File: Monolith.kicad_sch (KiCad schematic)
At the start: 22 parts, among them J2 Conn_01x11, J3 Conn_01x11, J4 Conn_01x02, J5 Conn_01x02, J7 Conn_01x08, U1 ADS1299IPAGR, U12 ESP32-S3-MINI-1

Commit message: Replace volt reg
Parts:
- C3: footprint (none) -> Capacitor_SMD:C_0603_1608Metric
- R6: footprint (none) -> Resistor_SMD:R_0603_1608Metric
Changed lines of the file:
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@@
       (effects (font (size 1.27 1.27)) (justify left))
     )
-    (property "Footprint" "" (at 166.5224 43.0276 0)
+    (property "Footprint" "Capacitor_SMD:C_0603_1608Metric" (at 166.5224 43.0276 0)
       (effects (font (size 1.27 1.27)) hide)
     )
@@
       (effects (font (size 1.27 1.27)) (justify left))
     )
-    (property "Footprint" "" (at 163.5252 25.5524 90)
-      (effects (font (size 1.27 1.27)) hide)
-    )
+    (property "Footprint" "Resistor_SMD:R_0603_1608Metric" (at 163.5252 25.5524 90)
+      (effects (font (size 1.27 1.27)) hide)
+    )

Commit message: fixes
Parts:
- C20: value 1uF -> 0.1uF; LCSC C15849 -> C3011705
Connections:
- net AVSS: now also C32.1, C33.1, U1.25 (VREFN)
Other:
- moved on the sheet: C32, C33

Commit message: new fixes
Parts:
- added C4: 0.1uF, Capacitor_SMD:C_0603_1608Metric, symbol Device:C
- added C5: 1uF, Capacitor_SMD:C_0603_1608Metric, symbol Device:C
- added S1, S2: TS-1187A-B-A-B, TS-1187A-B-A-B:SW_TS-1187A-B-A-B, symbol TS-1187A-B-A-B:TS-1187A-B-A-B
- C1, C33: LCSC C1691 -> C96446
- C19: footprint Capacitor_SMD:C_0805_2012Metric -> Capacitor_SMD:C_1206_3216Metric; LCSC C141660 -> C15008
- C2, C20, C32, C34: LCSC C3011705 -> C14663
- C56: LCSC C106205 -> C1523
- R6: LCSC C98220 -> C25804
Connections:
- net GND: now also C4.1, C5.2, S2.C, S2.D
- net DN: now reaches U12.23 (GPIO19/U1RTS/ADC2_CH8/CLK_OUT2/USB_D-)
- net DP: now reaches U12.24 (GPIO20/U1CTS/ADC2_CH9/CLK_OUT1/USB_D+)
- net EN: no longer names the net of C3.1, R6.2, U12.45 (EN)
- net EN: now also S1.C, S1.D
- net GPIO0: no longer names the net of U12.4 (GPIO0/BOOT)
- net GPIO0: now also C4.2, S2.A, S2.B
- new net: C5.1, S1.A, S1.B
- no-connect marks 38 -> 36
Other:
- sheet USB Port ports: added DN, DP; removed CHIP_PU, IO0, RX, TX

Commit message: fix pin headers
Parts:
- J2, J3: footprint Connector_PinSocket_2.54mm:PinSocket_1x11_P2.54mm_Vertical -> Connector_PinHeader_2.54mm:PinHeader_1x11_P2.54mm_Vertical
- J4, J5: footprint Connector_PinSocket_2.54mm:PinSocket_1x02_P2.54mm_Vertical -> Connector_PinHeader_2.54mm:PinHeader_1x02_P2.54mm_Vertical
- J7: footprint Connector_PinHeader_2.54mm:PinHeader_1x08_P2.54mm_Vertical -> Connector_PinSocket_2.54mm:PinSocket_1x08_P2.54mm_Vertical
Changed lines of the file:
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@@
       (effects (font (size 1.27 1.27)) (justify left))
     )
-    (property "Footprint" "Connector_PinHeader_2.54mm:PinHeader_1x08_P2.54mm_Vertical" (at 264.795 152.4 0)
+    (property "Footprint" "Connector_PinSocket_2.54mm:PinSocket_1x08_P2.54mm_Vertical" (at 264.795 152.4 0)
       (effects (font (size 1.27 1.27)) hide)
     )
@@
       (effects (font (size 1.27 1.27)) (justify left))
     )
-    (property "Footprint" "Connector_PinSocket_2.54mm:PinSocket_1x02_P2.54mm_Vertical" (at 28.575 55.245 0)
+    (property "Footprint" "Connector_PinHeader_2.54mm:PinHeader_1x02_P2.54mm_Vertical" (at 28.575 55.245 0)
       (effects (font (size 1.27 1.27)) hide)
     )
@@
       (effects (font (size 1.27 1.27)))
     )
-    (property "Footprint" "Connector_PinSocket_2.54mm:PinSocket_1x11_P2.54mm_Vertical" (at 41.275 36.83 0)
+    (property "Footprint" "Connector_PinHeader_2.54mm:PinHeader_1x11_P2.54mm_Vertical" (at 41.275 36.83 0)
       (effects (font (size 1.27 1.27)) hide)
     )
@@
       (effects (font (size 1.27 1.27)))
     )
-    (property "Footprint" "Connector_PinSocket_2.54mm:PinSocket_1x11_P2.54mm_Vertical" (at 29.21 36.83 0)
+    (property "Footprint" "Connector_PinHeader_2.54mm:PinHeader_1x11_P2.54mm_Vertical" (at 29.21 36.83 0)
       (effects (font (size 1.27 1.27)) hide)
     )
@@
       (effects (font (size 1.27 1.27)) (justify left))
     )
-    (property "Footprint" "Connector_PinSocket_2.54mm:PinSocket_1x02_P2.54mm_Vertical" (at 28.575 62.23 0)
-      (effects (font (size 1.27 1.27)) hide)
-    )
+    (property "Footprint" "Connector_PinHeader_2.54mm:PinHeader_1x02_P2.54mm_Vertical" (at 28.575 62.23 0)
+      (effects (font (size 1.27 1.27)) hide)
+    )

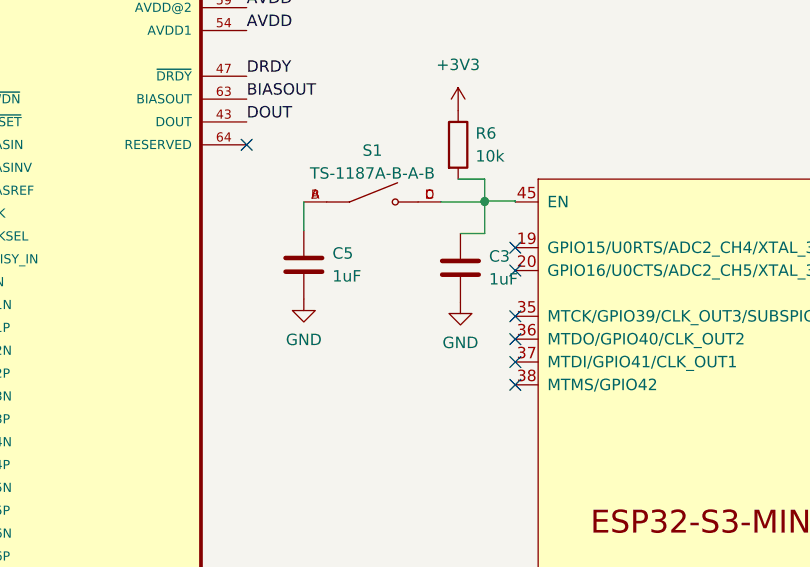
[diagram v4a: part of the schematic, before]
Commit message: fix reset button
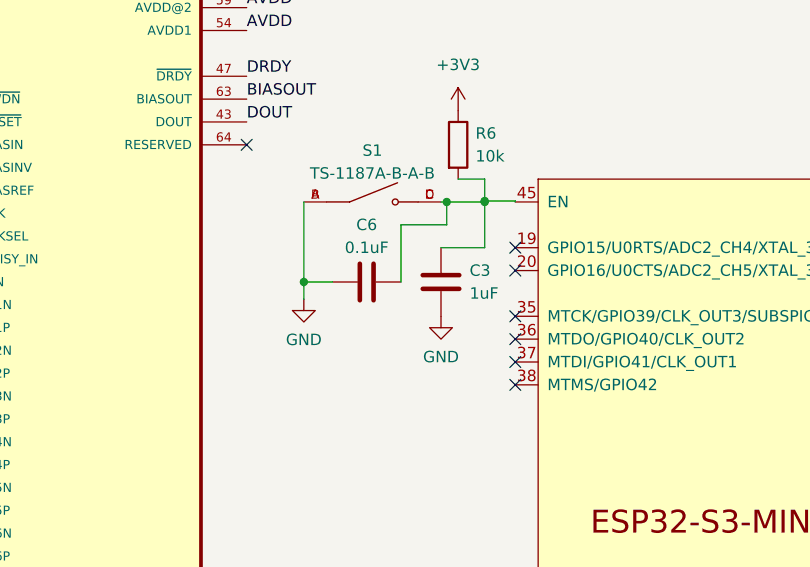
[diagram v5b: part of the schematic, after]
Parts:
- removed C5: 1uF, Capacitor_SMD:C_0603_1608Metric, symbol Device:C
- added C6: 0.1uF, Capacitor_SMD:C_0603_1608Metric, symbol Device:C
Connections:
- net GND: now also S1.A, S1.B, C6.2
- net at C3.1, R6.2, S1.C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: now also C6.1
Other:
- moved on the sheet: C3
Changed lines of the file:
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@@
   (junction (at 164.8714 53.34) (diameter 0) (color 0 0 0 0)
   )
+  (junction (at 144.78 62.23) (diameter 0) (color 0 0 0 0)
+  )
   (junction (at 164.8714 53.229) (diameter 0) (color 0 0 0 0)
   )
@@
   )
   (junction (at 74.93 50.165) (diameter 0) (color 0 0 0 0)
+  )
+  (junction (at 160.655 53.34) (diameter 0) (color 0 0 0 0)
   )
   (junction (at 144.78 143.51) (diameter 0) (color 0 0 0 0)
@@
     (stroke (width 0) (type default))
   )
+  (wire (pts (xy 160.655 55.88) (xy 155.575 55.88))
+    (stroke (width 0) (type default))
+  )
   (wire (pts (xy 261.62 68.58) (xy 259.715 68.58))
     (stroke (width 0) (type default))
   )
+  (wire (pts (xy 144.78 62.23) (xy 144.78 64.135))
+    (stroke (width 0) (type default))
+  )
   (wire (pts (xy 91.44 118.11) (xy 102.87 118.11))
     (stroke (width 0) (type default))
@@
     (stroke (width 0) (type default))
   )
-  (wire (pts (xy 164.8714 53.34) (xy 164.8714 56.8452))
+  (wire (pts (xy 164.8714 53.34) (xy 164.8714 58.42))
+    (stroke (width 0) (type default))
+  )
+  (wire (pts (xy 160.655 53.34) (xy 164.8714 53.34))
     (stroke (width 0) (type default))
   )
@@
     (stroke (width 0) (type default))
   )
+  (wire (pts (xy 147.955 62.23) (xy 144.78 62.23))
+    (stroke (width 0) (type default))
+  )
   (wire (pts (xy 213.995 31.75) (xy 213.995 43.18))
     (stroke (width 0) (type default))
@@
     (stroke (width 0) (type default))
   )
-  (wire (pts (xy 144.78 53.34) (xy 144.78 56.515))
+  (wire (pts (xy 144.78 53.34) (xy 144.78 62.23))
     (stroke (width 0) (type default))
   )
@@
     (stroke (width 0) (type default))
   )
-  (wire (pts (xy 162.179 56.8452) (xy 164.8714 56.8452))
+  (wire (pts (xy 160.02 58.42) (xy 164.8714 58.42))
+    (stroke (width 0) (type default))
+  )
+  (wire (pts (xy 155.575 55.88) (xy 155.575 62.23))
     (stroke (width 0) (type default))
   )
@@
     (stroke (width 0) (type default))
   )
+  (wire (pts (xy 160.655 53.34) (xy 160.655 55.88))
+    (stroke (width 0) (type default))
+  )
   (wire (pts (xy 164.8714 50.8) (xy 164.8714 53.229))
     (stroke (width 0) (type default))
@@
     (stroke (width 0) (type default))
   )
-  (wire (pts (xy 160.02 53.34) (xy 164.8714 53.34))
+  (wire (pts (xy 160.02 53.34) (xy 160.655 53.34))
     (stroke (width 0) (type default))
   )
@@
     )
   )
-  (symbol (lib_id "Device:C") (at 162.179 60.6552 0) (unit 1)
-    (in_bom yes) (on_board yes) (dnp no) (fields_autoplaced)
-    (property "Reference" "C3" (at 165.354 59.3852 0)
-      (effects (font (size 1.27 1.27)) (justify left))
-    )
-    (property "Value" "1uF" (at 165.354 61.9252 0)
-      (effects (font (size 1.27 1.27)) (justify left))
-    )
-    (property "Footprint" "Capacitor_SMD:C_0603_1608Metric" (at 163.1442 64.4652 0)
-      (effects (font (size 1.27 1.27)) hide)
-    )
-    (property "Datasheet" "~" (at 162.179 60.6552 0)
-      (effects (font (size 1.27 1.27)) hide)
-    )
-    (property "LCSC" "C15849" (at 162.179 60.6552 0)
+  (symbol (lib_id "Device:C") (at 160.02 62.23 0) (unit 1)
+    (in_bom yes) (on_board yes) (dnp no) (fields_autoplaced)
+    (property "Reference" "C3" (at 163.195 60.96 0)
+      (effects (font (size 1.27 1.27)) (justify left))
+    )
+    (property "Value" "1uF" (at 163.195 63.5 0)
+      (effects (font (size 1.27 1.27)) (justify left))
+    )
+    (property "Footprint" "Capacitor_SMD:C_0603_1608Metric" (at 160.9852 66.04 0)
+      (effects (font (size 1.27 1.27)) hide)
+    )
+    (property "Datasheet" "~" (at 160.02 62.23 0)
+      (effects (font (size 1.27 1.27)) hide)
+    )
+    (property "LCSC" "C15849" (at 160.02 62.23 0)
       (effects (font (size 1.27 1.27)) hide)
     )
@@
         (path "/a4ecfbe3-0f16-403e-8cdc-2760bb3b2c3f"
           (reference "C3") (unit 1)
+        )
+      )
+    )
+  )
+  (symbol (lib_id "Device:C") (at 151.765 62.23 270) (unit 1)
+    (in_bom yes) (on_board yes) (dnp no) (fields_autoplaced)
+    (property "Reference" "C6" (at 151.765 55.88 90)
+      (effects (font (size 1.27 1.27)))
+    )
+    (property "Value" "0.1uF" (at 151.765 58.42 90)
+      (effects (font (size 1.27 1.27)))
+    )
+    (property "Footprint" "Capacitor_SMD:C_0603_1608Metric" (at 147.955 63.1952 0)
+      (effects (font (size 1.27 1.27)) hide)
+    )
+    (property "Datasheet" "~" (at 151.765 62.23 0)
+      (effects (font (size 1.27 1.27)) hide)
+    )
+    (property "LCSC" "C14663" (at 151.765 62.23 90)
+      (effects (font (size 1.27 1.27)) hide)
+    )
+    (pin "1")
+    (pin "2")
+    (instances
+      (project "Monolith"
+        (path "/a4ecfbe3-0f16-403e-8cdc-2760bb3b2c3f"
+          (reference "C6") (unit 1)
         )
       )
@@
     )
   )
-  (symbol (lib_id "Device:C") (at 144.78 60.325 0) (unit 1)
-    (in_bom yes) (on_board yes) (dnp no) (fields_autoplaced)
-    (property "Reference" "C5" (at 147.955 59.055 0)
-      (effects (font (size 1.27 1.27)) (justify left))
-    )
-    (property "Value" "1uF" (at 147.955 61.595 0)
-      (effects (font (size 1.27 1.27)) (justify left))
-    )
-    (property "Footprint" "Capacitor_SMD:C_0603_1608Metric" (at 145.7452 64.135 0)
-      (effects (font (size 1.27 1.27)) hide)
-    )
-    (property "Datasheet" "~" (at 144.78 60.325 0)
-      (effects (font (size 1.27 1.27)) hide)
-    )
-    (property "LCSC" "C15849" (at 144.78 60.325 0)
-      (effects (font (size 1.27 1.27)) hide)
-    )
-    (pin "1")
-    (pin "2")
-    (instances
-      (project "Monolith"
-        (path "/a4ecfbe3-0f16-403e-8cdc-2760bb3b2c3f"
-          (reference "C5") (unit 1)
-        )
-      )
-    )
-  )
   (symbol (lib_id "Connector_Generic:Conn_01x11") (at 29.21 36.83 0) (unit 1)
     (in_bom yes) (on_board yes) (dnp no)
@@
     )
   )
-  (symbol (lib_id "power:GND") (at 162.179 64.4652 0) (unit 1)
-    (in_bom yes) (on_board yes) (dnp no) (fields_autoplaced)
-    (property "Reference" "#PWR014" (at 162.179 70.8152 0)
-      (effects (font (size 1.27 1.27)) hide)
-    )
-    (property "Value" "GND" (at 162.179 68.9864 0)
-      (effects (font (size 1.27 1.27)))
-    )
-    (property "Footprint" "" (at 162.179 64.4652 0)
-      (effects (font (size 1.27 1.27)) hide)
-    )
-    (property "Datasheet" "" (at 162.179 64.4652 0)
-      (effects (font (size 1.27 1.27)) hide)
-    )
+  (symbol (lib_id "power:GND") (at 160.02 66.04 0) (unit 1)
+    (in_bom yes) (on_board yes) (dnp no) (fields_autoplaced)
+    (property "Reference" "#PWR014" (at 160.02 72.39 0)
+      (effects (font (size 1.27 1.27)) hide)
+    )
+    (property "Value" "GND" (at 160.02 70.5612 0)
+      (effects (font (size 1.27 1.27)))
+    )
+    (property "Footprint" "" (at 160.02 66.04 0)
+      (effects (font (size 1.27 1.27)) hide)
+    )
+    (property "Datasheet" "" (at 160.02 66.04 0)
+      (effects (font (size 1.27 1.27)) hide)
+    )
